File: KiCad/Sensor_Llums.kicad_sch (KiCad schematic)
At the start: 4 parts, among them U3 RPR-0521RS

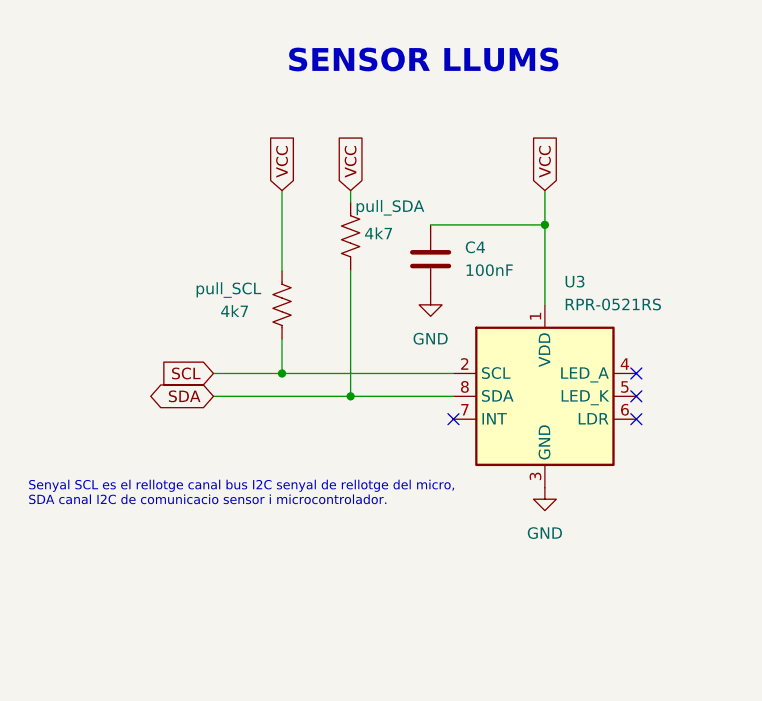
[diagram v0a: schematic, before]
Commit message: acabar can, estil y micro biel
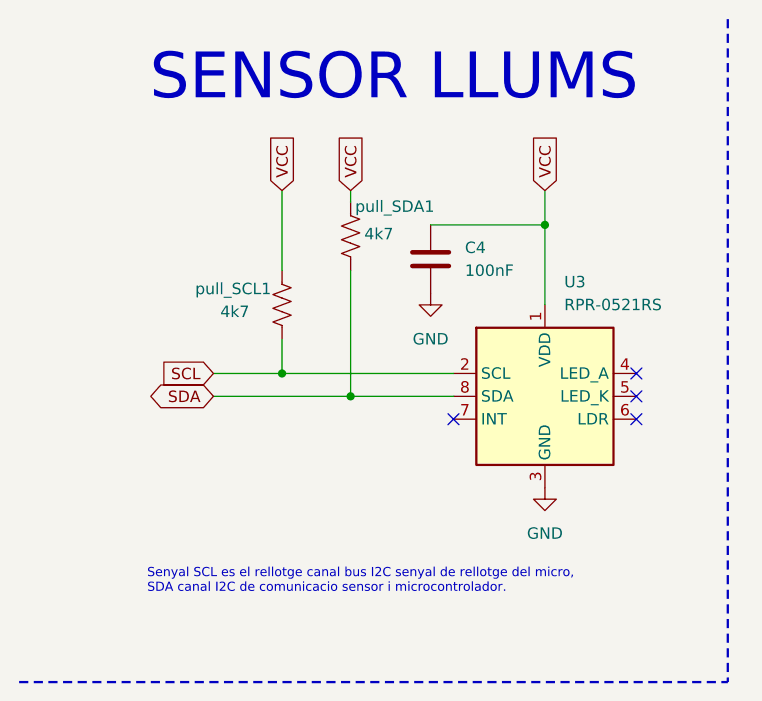
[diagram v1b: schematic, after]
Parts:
- renumbered pull_SCL to pull_SCL1, pull_SDA to pull_SDA1
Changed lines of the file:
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@@
 	(text "Senyal SCL es el rellotge canal bus I2C senyal de rellotge del micro,\nSDA canal I2C de comunicacio sensor i microcontrolador."
 		(exclude_from_sim no)
-		(at 13.716 65.532 0)
+		(at 26.924 75.184 0)
 		(effects
 			(font
 				(size 1.016 1.016)
+				(color 0 0 0 1)
 			)
 			(justify left)
 		)
 	)
-	(text "SENSOR LLUMS\n"
-		(exclude_from_sim no)
-		(at 57.658 17.526 0)
+	(text "SENSOR LLUMS\n\n"
+		(exclude_from_sim no)
+		(at 54.356 23.368 0)
 		(effects
 			(font
-				(size 2.54 2.54)
-				(thickness 0.254)
-				(bold yes)
+				(size 5.08 5.08)
+				(color 0 0 0 1)
 			)
 		)
@@
 			(width 0)
 			(type default)
+		)
+	)
+	(polyline
+		(pts
+			(xy 12.7 86.36) (xy 91.44 86.36)
+		)
+		(stroke
+			(width 0.254)
+			(type dash)
+			(color 0 0 0 1)
+		)
+	)
+	(polyline
+		(pts
+			(xy 91.44 12.7) (xy 91.44 86.36)
+		)
+		(stroke
+			(width 0.254)
+			(type dash)
+			(color 0 0 0 1)
 		)
 	)
@@
 		(on_board yes)
 		(dnp no)
-		(property "Reference" "pull_SCL"
+		(property "Reference" "pull_SCL1"
 			(at 32.258 42.672 0)
 			(effects
@@
 			(project ""
 				(path "/88ef36bc-9439-47f2-adb5-e1da6bb8c9dd/8bdb4d91-b6d7-45e8-b65e-8d615eba0b9e"
-					(reference "pull_SCL")
+					(reference "pull_SCL1")
 					(unit 1)
 				)
@@
 		(on_board yes)
 		(dnp no)
-		(property "Reference" "pull_SDA"
+		(property "Reference" "pull_SDA1"
 			(at 50.038 33.528 0)
 			(effects
@@
 			(project "Grup_D_Llums"
 				(path "/88ef36bc-9439-47f2-adb5-e1da6bb8c9dd/8bdb4d91-b6d7-45e8-b65e-8d615eba0b9e"
-					(reference "pull_SDA")
+					(reference "pull_SDA1")
 					(unit 1)
 				)
